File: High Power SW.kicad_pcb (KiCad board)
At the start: 2 copper layers, 48 x 36 mm, 21 parts, among them CN1 Jumper_NC_Small, Q1 PSMN5R6-60YLX, U1 PS2801C-1-A

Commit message: Updtes for Manufacture
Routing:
- net +BATT: track 28.3 -> 23.3 mm, vias 0 -> 1
- net Net-(JP1-Pad2): track 13.3 -> 9.93 mm
- net GND: track 38.4 -> 37.3 mm
- net Net-(R1-Pad1): track 18.7 -> 17.5 mm
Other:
- net class Default: clearance 0.2 -> 0.3048
- net class Power: clearance 0.2 -> 0.3048
- net class small_trace: clearance 0.2 -> 0.3048
- rule trace_clearance: 0.2 -> 0.3048

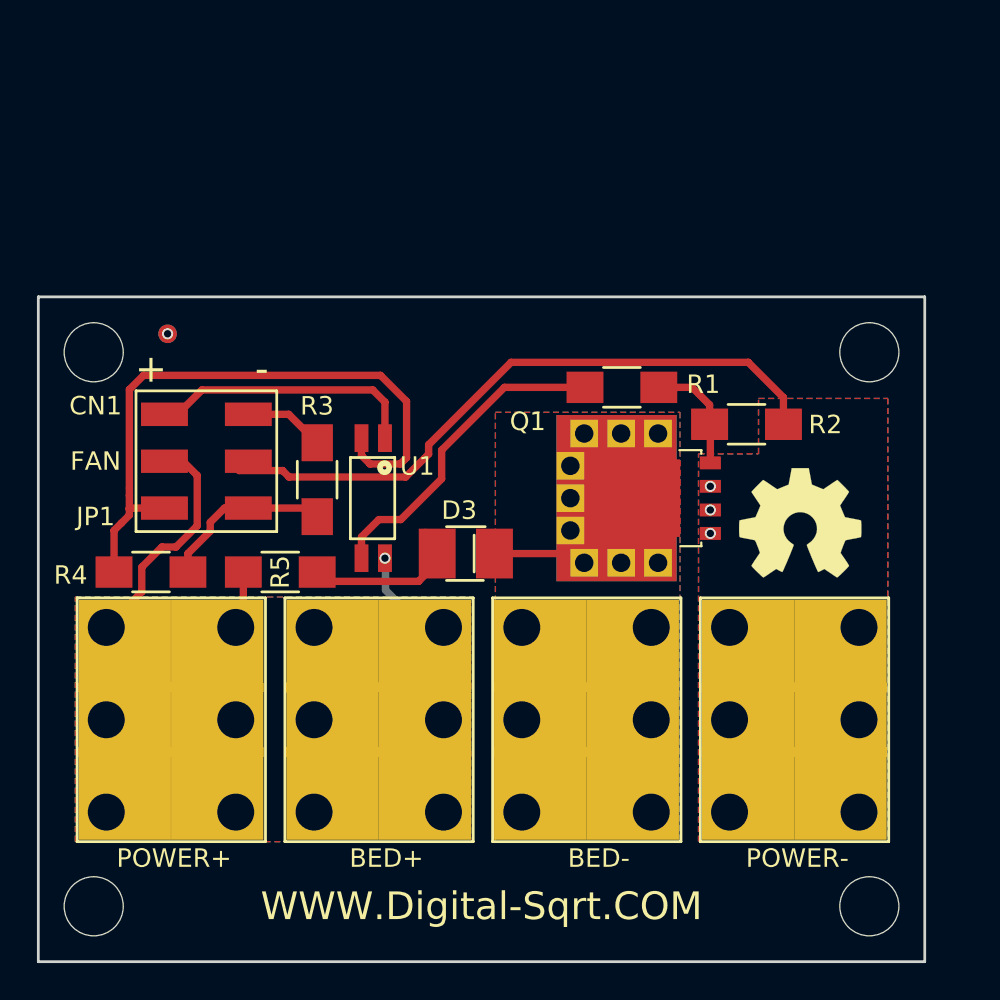
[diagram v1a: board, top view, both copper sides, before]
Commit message: Make board 5x5
5cm by 5cm boards are lower cost
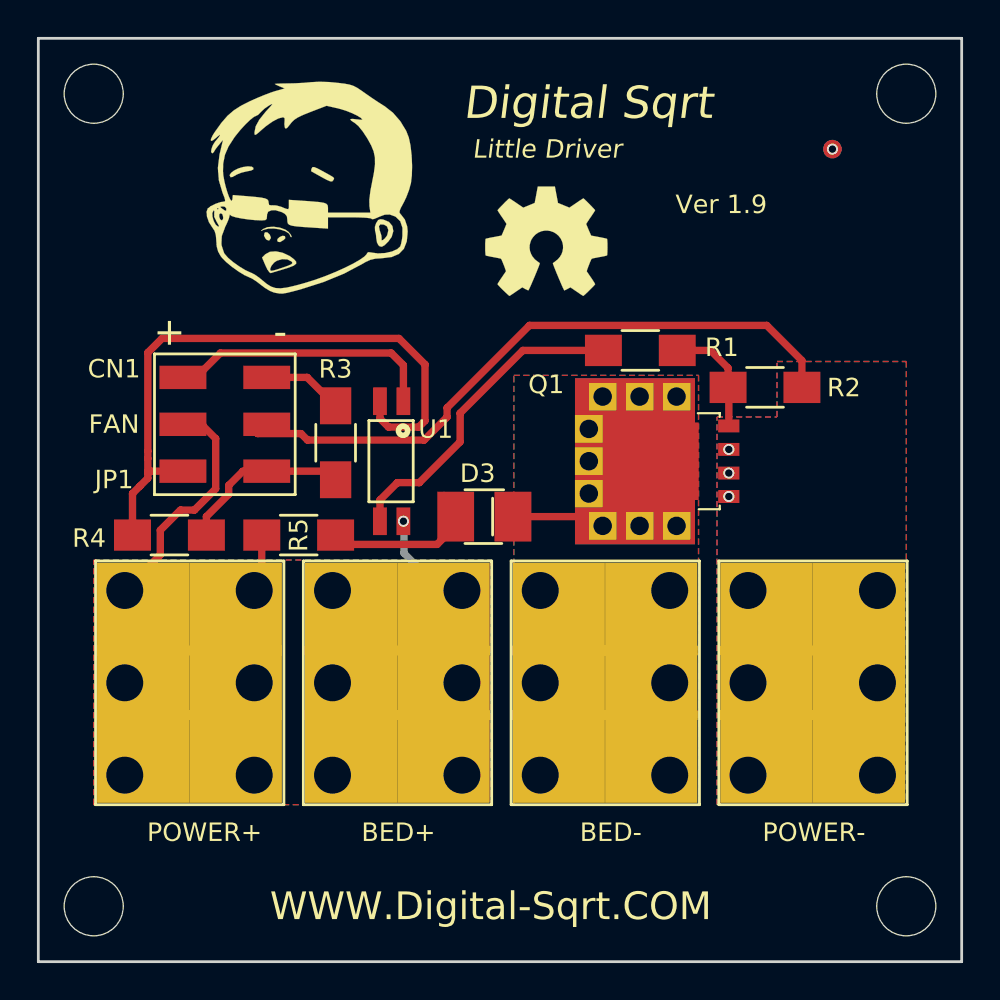
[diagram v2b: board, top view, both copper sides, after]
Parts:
- ?: moved to F.Cu
- moved F1  37.4 mm to (110.0, 95.0) (x2)
- moved REF*** 20.5 mm to (94.5, 100.0)
- moved ? 17.4 mm to (81.5, 97.0), turned to 0 degrees
- moved ? 14.1 mm to (114.0, 92.0)
- moved ? 14.0 mm to (70.0, 92.0)
- moved BED+ 2.24 mm to (86.3, 123.9)
- moved BED- 2.24 mm to (97.6, 123.9)
- moved CN1 2.24 mm to (77.1, 109.9)
- moved D3 2.24 mm to (91.1, 114.9)
- moved POWER+ 2.24 mm to (75.1, 123.9)
- moved POWER- 2.24 mm to (108.8, 123.9)
- moved Q1 2.24 mm to (100.6, 111.9)
- moved R1 2.24 mm to (99.6, 105.9)
- moved R2 2.24 mm to (106.3, 107.9)
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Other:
- board size 48 x 36 mm -> 50 x 50 mm
- board text added: "Ver 1.9"
- board text removed: "Ver 1.8"

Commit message: Update for improved Manufacture
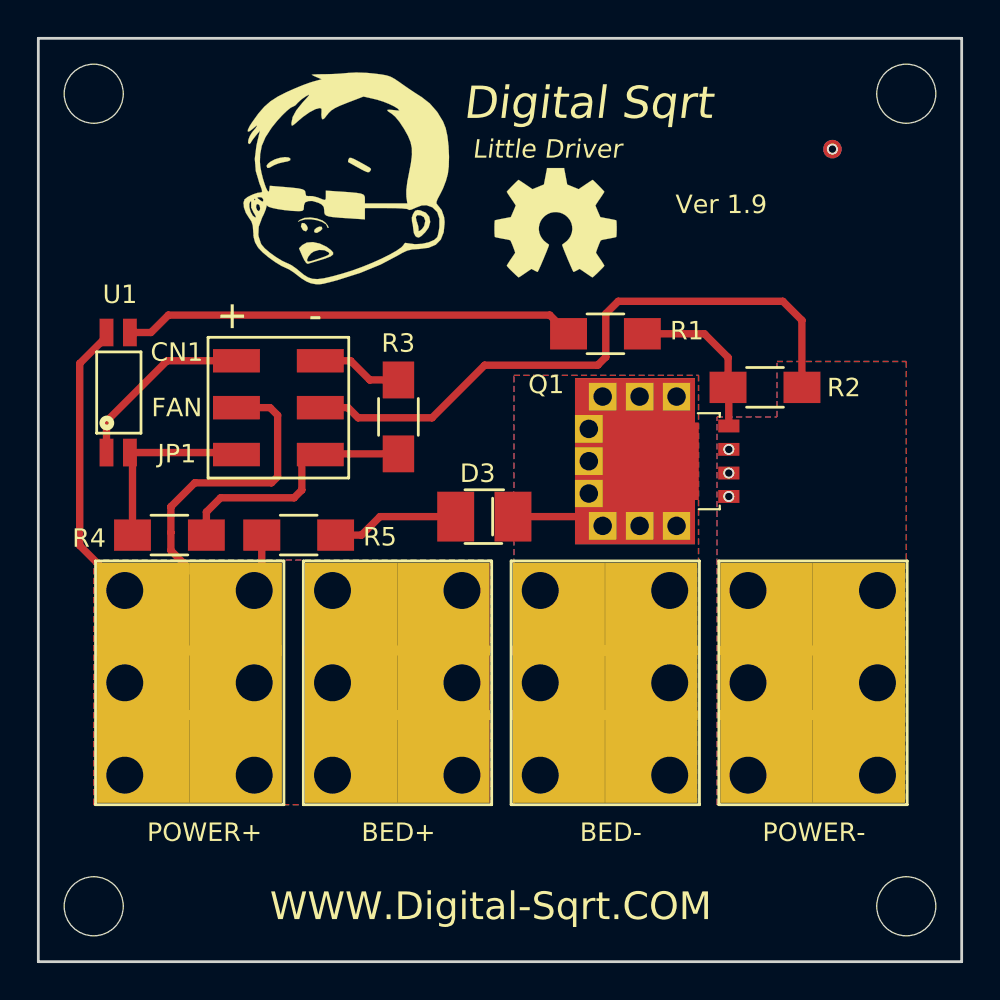
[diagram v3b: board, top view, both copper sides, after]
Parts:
- moved U1 15.2 mm to (71.4, 108.2), turned to 90 degrees
- moved R3 3.68 mm to (86.5, 109.5)
- moved CN1 3.04 mm to (80.0, 109.0)
- moved R1 2.09 mm to (97.7, 105.0)
- moved ? 2.06 mm to (83.5, 96.5)
- moved REF*** 1.12 mm to (95.0, 99.0)
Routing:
- net Net-(JP1-Pad1): track 37.8 -> 11.3 mm
- net +BATT: track 23.3 -> 38.4 mm, vias 1 -> 0
- net Net-(R1-Pad1): track 17.5 -> 24.6 mm
- net Net-(JP1-Pad2): track 9.93 -> 14.3 mm
- net Net-(CN1-Pad1): track 13.9 -> 11.1 mm
- net Net-(Q1-Pad4): track 6.30 -> 8.90 mm
- net GND: track 37.3 -> 35.6 mm
- net Net-(D3-Pad2): track 9.71 -> 8.38 mm

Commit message: Update opto footprint and add logos
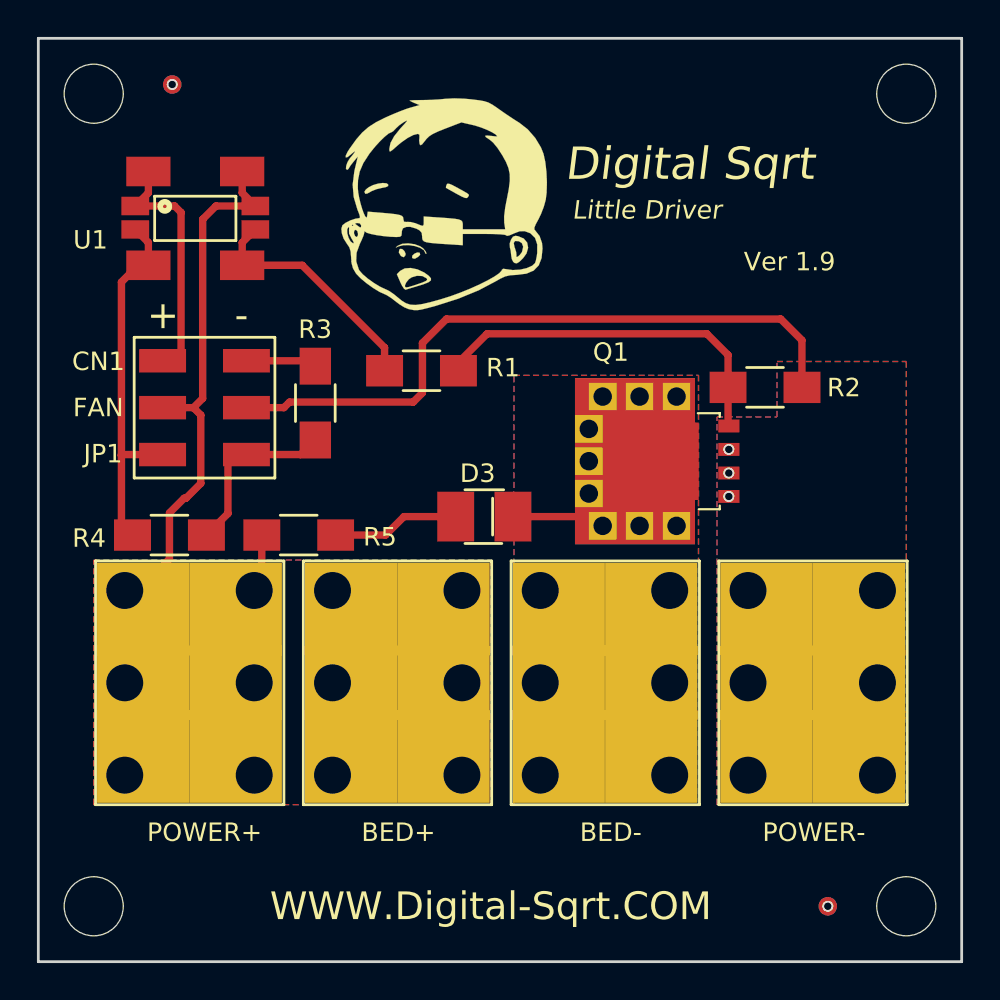
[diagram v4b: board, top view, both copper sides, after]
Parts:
- added ?: , MyLib:LOGO_POS, B.Cu at (106.0, 98.5)
- added ?: Symbol_CreativeCommons_CopperTop_Type2_Small, Symbols:Symbol_CreativeCommons_CopperTop_Type2_Small, B.Cu at (84.0, 110.5)
- added ?: Symbol_CC-Attribution_CopperTop_Small, Symbols:Symbol_CC-Attribution_CopperTop_Small, B.Cu at (72.0, 110.5)
- added ?: Symbol_CC-ShareAlike_CopperTop_Small, Symbols:Symbol_CC-ShareAlike_CopperTop_Small, B.Cu at (78.0, 110.5)
- added ?: , Fiducials:Fiducial_1mm_Dia_2.54mm_Outer_CopperTop, F.Cu at (109.8, 136.0)
- added ?: , Fiducials:Fiducial_1mm_Dia_2.54mm_Outer_CopperTop, B.Cu at (109.8, 136.0)
- ? (x2): renamed from F1 
- ?: renamed from REF***; moved to B.Cu
- U1: footprint MyLib:SOP-4 -> MyLib:OP_Hybrid
- moved ? 35.9 mm to (74.2, 91.5) (x2)
- moved ? 11.7 mm to (91.0, 110.0), turned to 180 degrees
- moved U1 10.3 mm to (75.5, 98.8), turned to 0 degrees
- moved R1 10.2 mm to (87.8, 107.0)
- moved ? 5.48 mm to (88.8, 97.9)
- moved R3 4.56 mm to (82.0, 108.8)
- moved CN1 4.00 mm to (76.0, 109.0)
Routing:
- net Net-(R1-Pad1): track 24.6 -> 13.0 mm
- net Net-(Q1-Pad4): track 8.90 -> 20.1 mm
- net Net-(JP1-Pad1): track 11.3 -> 21.5 mm
- net +BATT: track 38.4 -> 32.4 mm
- net Net-(JP1-Pad2): track 14.3 -> 10.2 mm
- net GND: track 35.6 -> 37.9 mm, vias 4 -> 5
- net Net-(CN1-Pad1): track 11.1 -> 12.8 mm
- net Net-(CN1-Pad2): track 5.66 -> 4.85 mm
- net Net-(D3-Pad2): track 8.38 -> 7.66 mm
